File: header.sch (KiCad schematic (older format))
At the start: 43 parts, among them J1 Conn_01x10, J2 Conn_01x08, J3 Conn_01x06, J4 Conn_01x08, Q2 Q_NMOS_GSD, Q3 Q_NMOS_GSD, Q4 Q_NMOS_GSD, SW6 SW_Push, U1 ICE40HX4K-TQ144, U20 MAX11614, U22 MAX40200AUK, U8 TXS0108EPW, U9 TXS0108EPW, Y2 ECS-3225S33-500-FN-TR

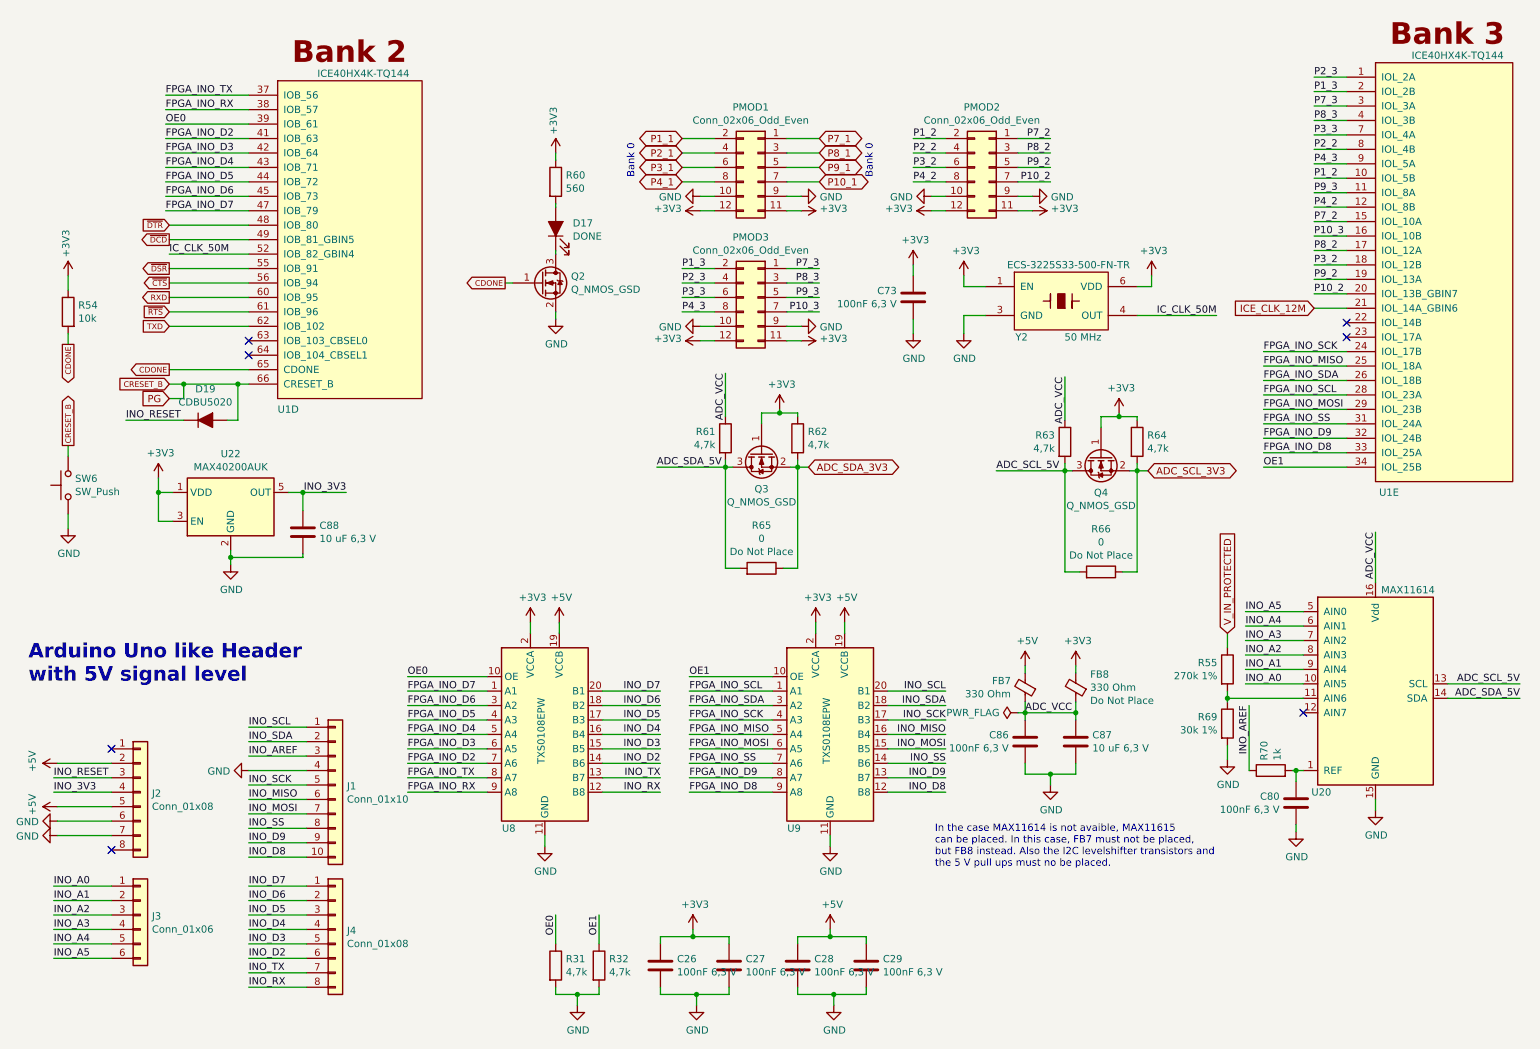
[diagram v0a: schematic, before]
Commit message: Finished Silkscreen and added layer markings as specified by manufacturer
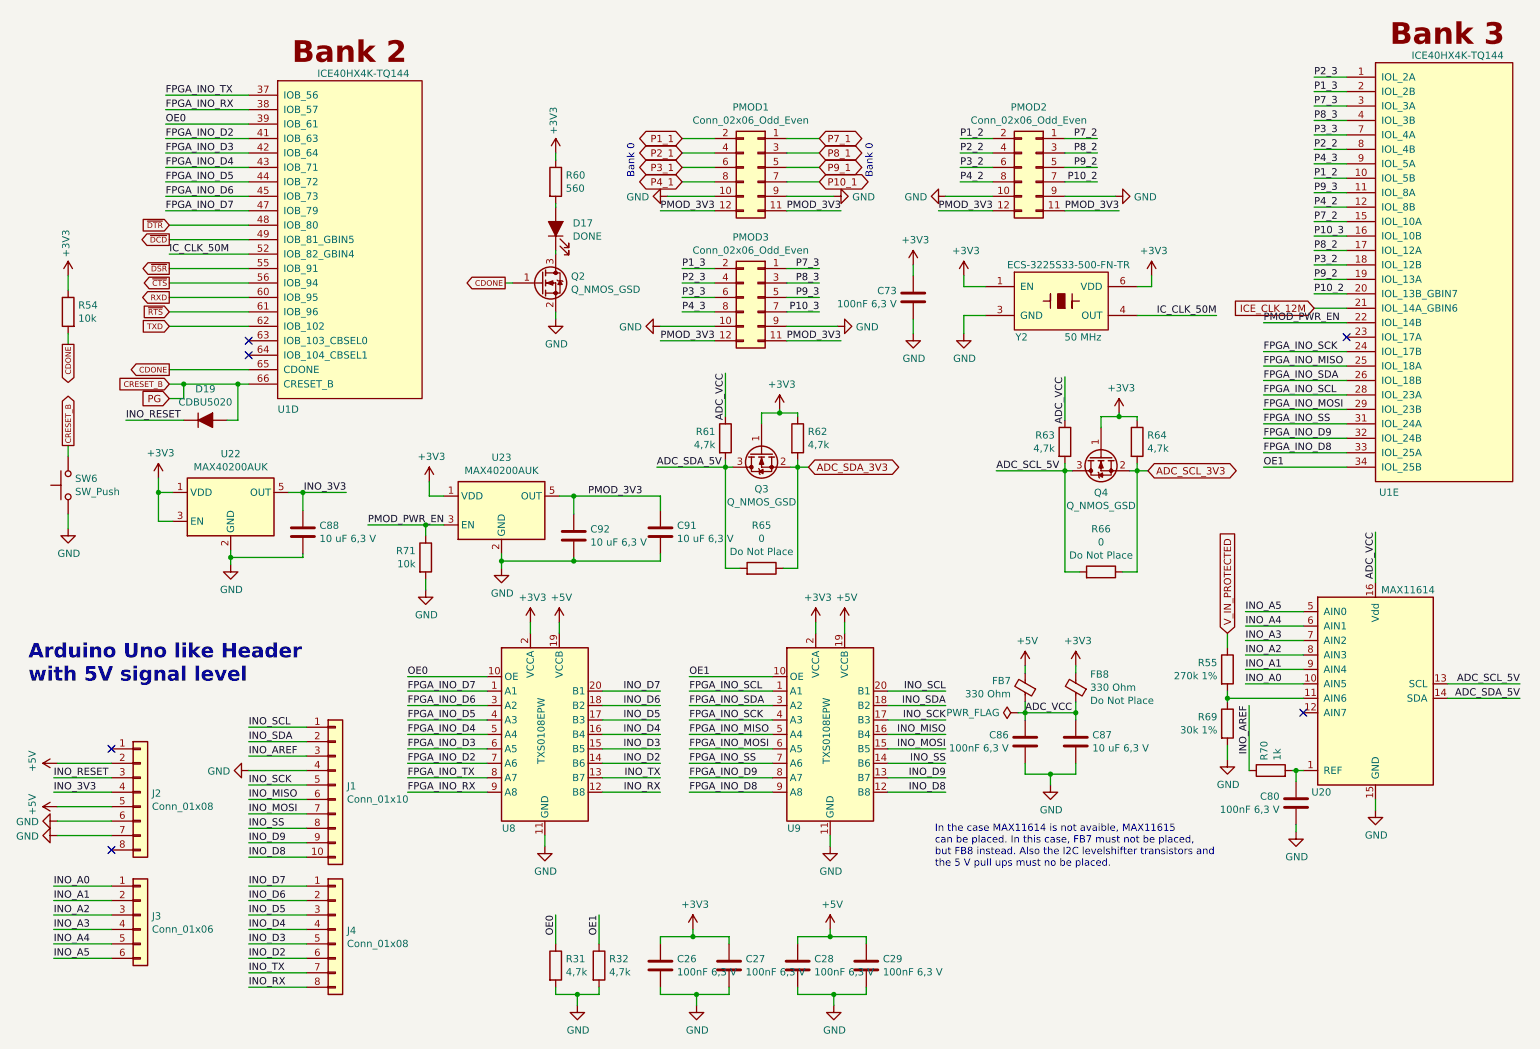
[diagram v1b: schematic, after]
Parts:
- added C91, C92: 10 uF 6,3 V, Capacitor_SMD:C_0603_1608Metric, symbol Device:C
- added R71: 10k, Resistor_SMD:R_0603_1608Metric, symbol Device:R
- added U23: MAX40200AUK, Package_TO_SOT_SMD:SOT-23-5, symbol Analog_Switch:MAX40200AUK
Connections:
- net +3V3: now also U23.1 (VDD); no longer PMOD1.11 (Pin_11), PMOD1.12 (Pin_12), PMOD2.11 (Pin_11), PMOD2.12 (Pin_12), PMOD3.11 (Pin_11), PMOD3.12 (Pin_12)
- net GND: now also C91.2, C92.2, R71.2, U23.2 (GND)
- net PMOD_PWR_EN: now reaches U1.22 (IOL_14B)
- net PMOD_PWR_EN: now also R71.1, U23.3 (EN)
- new net PMOD_3V3: C91.1, C92.1, PMOD1.11 (Pin_11), PMOD1.12 (Pin_12), PMOD2.11 (Pin_11), PMOD2.12 (Pin_12), PMOD3.11 (Pin_11), PMOD3.12 (Pin_12), U23.5 (OUT)
- no-connect marks 7 -> 6
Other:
- moved on the sheet: PMOD2

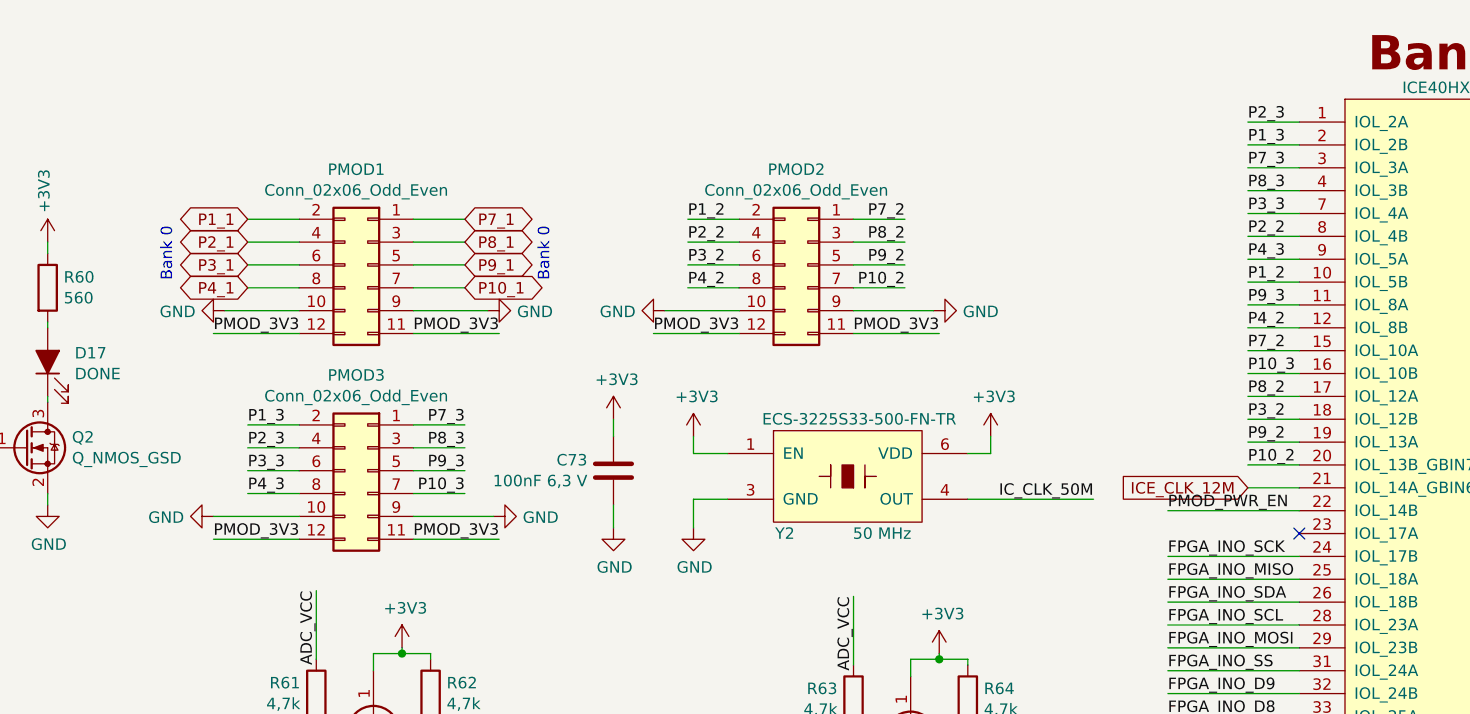
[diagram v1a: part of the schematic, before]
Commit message: Fixed rotated PMODs
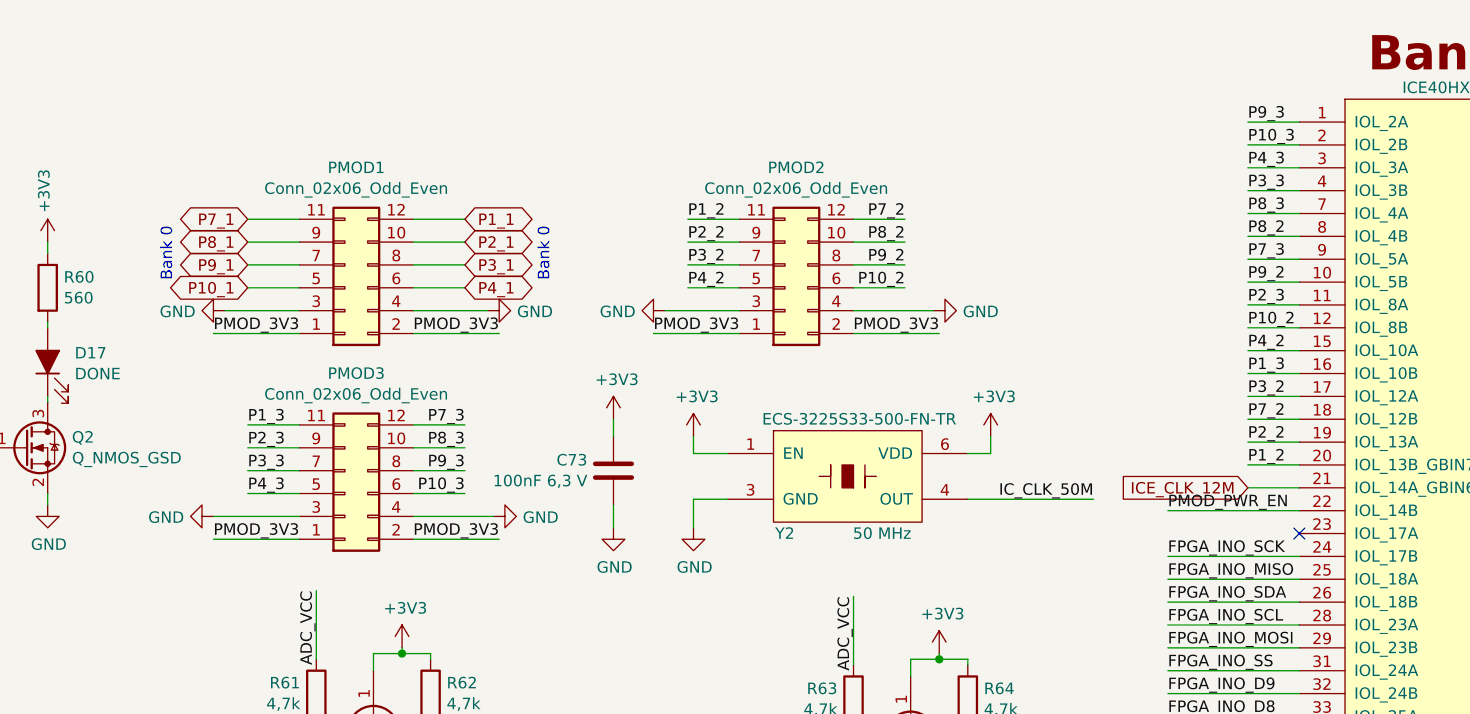
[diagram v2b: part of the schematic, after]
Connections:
- net GND: now also PMOD1.3 (Pin_3), PMOD1.4 (Pin_4), PMOD2.3 (Pin_3), PMOD2.4 (Pin_4), PMOD3.3 (Pin_3), PMOD3.4 (Pin_4); no longer PMOD1.10 (Pin_10), PMOD1.9 (Pin_9), PMOD2.10 (Pin_10), PMOD2.9 (Pin_9), PMOD3.10 (Pin_10), PMOD3.9 (Pin_9)
- net P10_1: now also PMOD1.5 (Pin_5); no longer PMOD1.7 (Pin_7)
- net P10_2: now also PMOD2.6 (Pin_6), U1.12 (IOL_8B); no longer PMOD2.7 (Pin_7), U1.20 (IOL_13B_GBIN7)
- net P10_3: now also PMOD3.6 (Pin_6), U1.2 (IOL_2B); no longer PMOD3.7 (Pin_7), U1.16 (IOL_10B)
- net P1_1: now also PMOD1.12 (Pin_12); no longer PMOD1.2 (Pin_2)
- net P1_2: now also PMOD2.11 (Pin_11), U1.20 (IOL_13B_GBIN7); no longer PMOD2.2 (Pin_2), U1.10 (IOL_5B)
- net P1_3: now also PMOD3.11 (Pin_11), U1.16 (IOL_10B); no longer PMOD3.2 (Pin_2), U1.2 (IOL_2B)
- net P2_1: now also PMOD1.10 (Pin_10); no longer PMOD1.4 (Pin_4)
- net P2_2: now also PMOD2.9 (Pin_9), U1.19 (IOL_13A); no longer PMOD2.4 (Pin_4), U1.8 (IOL_4B)
- net P2_3: now also PMOD3.9 (Pin_9), U1.11 (IOL_8A); no longer PMOD3.4 (Pin_4), U1.1 (IOL_2A)
- net P3_1: now also PMOD1.8 (Pin_8); no longer PMOD1.6 (Pin_6)
- net P3_2: now also PMOD2.7 (Pin_7), U1.17 (IOL_12A); no longer PMOD2.6 (Pin_6), U1.18 (IOL_12B)
- net P3_3: now also PMOD3.7 (Pin_7), U1.4 (IOL_3B); no longer PMOD3.6 (Pin_6), U1.7 (IOL_4A)
- net P4_1: now also PMOD1.6 (Pin_6); no longer PMOD1.8 (Pin_8)
- net P4_2: now also PMOD2.5 (Pin_5), U1.15 (IOL_10A); no longer PMOD2.8 (Pin_8), U1.12 (IOL_8B)
- net P4_3: now also PMOD3.5 (Pin_5), U1.3 (IOL_3A); no longer PMOD3.8 (Pin_8), U1.9 (IOL_5A)
- net P7_1: now also PMOD1.11 (Pin_11); no longer PMOD1.1 (Pin_1)
- net P7_2: now also PMOD2.12 (Pin_12), U1.18 (IOL_12B); no longer PMOD2.1 (Pin_1), U1.15 (IOL_10A)
- net P7_3: now also PMOD3.12 (Pin_12), U1.9 (IOL_5A); no longer PMOD3.1 (Pin_1), U1.3 (IOL_3A)
- net P8_1: now also PMOD1.9 (Pin_9); no longer PMOD1.3 (Pin_3)
- net P8_2: now also PMOD2.10 (Pin_10), U1.8 (IOL_4B); no longer PMOD2.3 (Pin_3), U1.17 (IOL_12A)
- net P8_3: now also PMOD3.10 (Pin_10), U1.7 (IOL_4A); no longer PMOD3.3 (Pin_3), U1.4 (IOL_3B)
- net P9_1: now also PMOD1.7 (Pin_7); no longer PMOD1.5 (Pin_5)
- net P9_2: now also PMOD2.8 (Pin_8), U1.10 (IOL_5B); no longer PMOD2.5 (Pin_5), U1.19 (IOL_13A)
- net P9_3: now also PMOD3.8 (Pin_8), U1.1 (IOL_2A); no longer PMOD3.5 (Pin_5), U1.11 (IOL_8A)
- net PMOD_3V3: now also PMOD1.1 (Pin_1), PMOD1.2 (Pin_2), PMOD2.1 (Pin_1), PMOD2.2 (Pin_2), PMOD3.1 (Pin_1), PMOD3.2 (Pin_2); no longer PMOD1.11 (Pin_11), PMOD1.12 (Pin_12), PMOD2.11 (Pin_11), PMOD2.12 (Pin_12), PMOD3.11 (Pin_11), PMOD3.12 (Pin_12)
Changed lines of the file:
@@
 	0    -1   1    0
 $EndComp
-Wire Wire Line
-	6375 1800 6050 1800
 $Comp
 L power:GND #PWR053
@@
 	5225 1800 5550 1800
 $Comp
-L Connector_Generic:Conn_02x06_Odd_Even PMOD1
-U 1 1 5CD7A9BF
-P 5850 1600
-F 0 "PMOD1" H 5900 2017 50  0000 C CNN
-F 1 "Conn_02x06_Odd_Even" H 5900 1926 50  0000 C CNN
-F 2 "Connector_PinSocket_2.54mm:PinSocket_2x06_P2.54mm_Horizontal" H 5850 1600 50  0001 C CNN
-F 3 "~" H 5850 1600 50  0001 C CNN
-	1    5850 1600
-	-1   0    0    -1
-$EndComp
-Wire Wire Line
-	5325 1400 5550 1400
-Wire Wire Line
-	5325 1500 5550 1500
-Wire Wire Line
-	5325 1600 5550 1600
-Wire Wire Line
-	5325 1700 5550 1700
-Wire Wire Line
-	6275 1400 6050 1400
-Wire Wire Line
-	6275 1500 6050 1500
-Wire Wire Line
-	6275 1600 6050 1600
-Wire Wire Line
-	6275 1700 6050 1700
-$Comp
 L power:GND #PWR056
 U 1 1 5CDD8FE0
@@
 L Connector_Generic:Conn_02x06_Odd_Even PMOD2
 U 1 1 5CDD9002
-P 7775 1600
-F 0 "PMOD2" H 7825 2017 50  0000 C CNN
-F 1 "Conn_02x06_Odd_Even" H 7825 1926 50  0000 C CNN
-F 2 "Connector_PinSocket_2.54mm:PinSocket_2x06_P2.54mm_Horizontal" H 7775 1600 50  0001 C CNN
-F 3 "~" H 7775 1600 50  0001 C CNN
-	1    7775 1600
-	-1   0    0    -1
+P 7675 1700
+F 0 "PMOD2" H 7725 1175 50  0000 C CNN
+F 1 "Conn_02x06_Odd_Even" H 7725 1266 50  0000 C CNN
+F 2 "Connector_PinSocket_2.54mm:PinSocket_2x06_P2.54mm_Horizontal" H 7675 1700 50  0001 C CNN
+F 3 "~" H 7675 1700 50  0001 C CNN
+	1    7675 1700
+	1    0    0    1
 $EndComp
 Wire Wire Line
@@
 L Connector_Generic:Conn_02x06_Odd_Even PMOD3
 U 1 1 5CDF4279
-P 5850 2500
-F 0 "PMOD3" H 5900 2917 50  0000 C CNN
-F 1 "Conn_02x06_Odd_Even" H 5900 2826 50  0000 C CNN
-F 2 "Connector_PinSocket_2.54mm:PinSocket_2x06_P2.54mm_Horizontal" H 5850 2500 50  0001 C CNN
-F 3 "~" H 5850 2500 50  0001 C CNN
-	1    5850 2500
-	-1   0    0    -1
+P 5750 2600
+F 0 "PMOD3" H 5800 2075 50  0000 C CNN
+F 1 "Conn_02x06_Odd_Even" H 5800 2166 50  0000 C CNN
+F 2 "Connector_PinSocket_2.54mm:PinSocket_2x06_P2.54mm_Horizontal" H 5750 2600 50  0001 C CNN
+F 3 "~" H 5750 2600 50  0001 C CNN
+	1    5750 2600
+	1    0    0    1
 $EndComp
 Text Label 5325 2300 0    50   ~ 0
@@
 Wire Wire Line
 	6275 2600 6050 2600
+Text Label 9700 2375 0    50   ~ 0
+P2_2
+Wire Wire Line
+	9700 2375 9925 2375
+Text Label 9700 2175 0    50   ~ 0
+P3_2
+Wire Wire Line
+	9700 2175 9925 2175
+Text Label 9700 1975 0    50   ~ 0
+P4_2
+Wire Wire Line
+	9700 1975 9925 1975
+Text Label 9700 2275 0    50   ~ 0
+P7_2
+Wire Wire Line
+	9700 2275 9925 2275
+Text Label 9700 1475 0    50   ~ 0
+P8_2
+Wire Wire Line
+	9700 1475 9925 1475
 Text Label 9700 1675 0    50   ~ 0
-P1_2
+P9_2
 Wire Wire Line
 	9700 1675 9925 1675
-Text Label 9700 1475 0    50   ~ 0
-P2_2
-Wire Wire Line
-	9700 1475 9925 1475
-Text Label 9700 2275 0    50   ~ 0
-P3_2
-Wire Wire Line
-	9700 2275 9925 2275
-Text Label 9700 1875 0    50   ~ 0
-P4_2
-Wire Wire Line
-	9700 1875 9925 1875
-Text Label 9700 1975 0    50   ~ 0
-P7_2
-Wire Wire Line
-	9700 1975 9925 1975
-Text Label 9700 2175 0    50   ~ 0
-P8_2
-Wire Wire Line
-	9700 2175 9925 2175
-Text Label 9700 2375 0    50   ~ 0
-P9_2
-Wire Wire Line
-	9700 2375 9925 2375
+Text Label 9700 2075 0    50   ~ 0
+P1_3
+Wire Wire Line
+	9700 2075 9925 2075
+Text Label 9700 1775 0    50   ~ 0
+P2_3
+Wire Wire Line
+	9700 1775 9925 1775
+Text Label 9700 1275 0    50   ~ 0
+P3_3
+Wire Wire Line
+	9700 1275 9925 1275
+Text Label 9700 1175 0    50   ~ 0
+P4_3
+Wire Wire Line
+	9700 1175 9925 1175
+Text Label 9700 1575 0    50   ~ 0
+P7_3
+Wire Wire Line
+	9700 1575 9925 1575
+Text Label 9700 1375 0    50   ~ 0
+P8_3
+Wire Wire Line
+	9700 1375 9925 1375
+Text Label 9700 975  0    50   ~ 0
+P9_3
+Wire Wire Line
+	9700 975  9925 975
 Text Label 9700 1075 0    50   ~ 0
-P1_3
+P10_3
 Wire Wire Line
 	9700 1075 9925 1075
-Text Label 9700 975  0    50   ~ 0
-P2_3
-Wire Wire Line
-	9700 975  9925 975
-Text Label 9700 1375 0    50   ~ 0
-P3_3
-Wire Wire Line
-	9700 1375 9925 1375
-Text Label 9700 1575 0    50   ~ 0
-P4_3
-Wire Wire Line
-	9700 1575 9925 1575
-Text Label 9700 1175 0    50   ~ 0
-P7_3
-Wire Wire Line
-	9700 1175 9925 1175
-Text Label 9700 1275 0    50   ~ 0
-P8_3
-Wire Wire Line
-	9700 1275 9925 1275
-Text Label 9700 1775 0    50   ~ 0
-P9_3
-Wire Wire Line
-	9700 1775 9925 1775
-Text Label 9700 2075 0    50   ~ 0
-P10_3
-Wire Wire Line
-	9700 2075 9925 2075
 Text GLabel 1775 2500 0    39   Output ~ 0
 RXD
@@
 Text Label 7250 1400 0    50   ~ 0
 P1_2
-Text GLabel 5325 1400 0    50   BiDi ~ 0
+Text GLabel 6275 1400 2    50   BiDi ~ 0
 P1_1
-Text GLabel 5325 1500 0    50   BiDi ~ 0
+Text GLabel 6275 1500 2    50   BiDi ~ 0
 P2_1
-Text GLabel 5325 1600 0    50   BiDi ~ 0
+Text GLabel 6275 1600 2    50   BiDi ~ 0
 P3_1
-Text GLabel 5325 1700 0    50   BiDi ~ 0
+Text GLabel 6275 1700 2    50   BiDi ~ 0
 P4_1
-Text GLabel 6275 1400 2    50   BiDi ~ 0
-P7_1
-Text GLabel 6275 1500 2    50   BiDi ~ 0
-P8_1
-Text GLabel 6275 1600 2    50   BiDi ~ 0
-P9_1
-Text GLabel 6275 1700 2    50   BiDi ~ 0
-P10_1
 Wire Wire Line
 	2325 2100 1775 2100
@@
 FPGA_INO_D2
 Wire Wire Line
-	9700 2475 9925 2475
-Text Label 9700 2475 0    50   ~ 0
+	9700 1875 9925 1875
+Text Label 9700 1875 0    50   ~ 0
 P10_2
 Text Label 5625 3025 3    50   ~ 0
@@
 Text Label 6425 1900 2    50   ~ 0
 PMOD_3V3
-Wire Wire Line
-	6050 1900 6425 1900
 Text Label 5175 1900 0    50   ~ 0
 PMOD_3V3
@@
 Wire Wire Line
 	3550 4525 3550 4450
+Text GLabel 5325 1700 0    50   BiDi ~ 0
+P10_1
+Text GLabel 5325 1600 0    50   BiDi ~ 0
+P9_1
+Text GLabel 5325 1500 0    50   BiDi ~ 0
+P8_1
+Text GLabel 5325 1400 0    50   BiDi ~ 0
+P7_1
+Wire Wire Line
+	5325 1700 5550 1700
+Wire Wire Line
+	5325 1600 5550 1600
+Wire Wire Line
+	5325 1500 5550 1500
+Wire Wire Line
+	5325 1400 5550 1400
+Wire Wire Line
+	9700 2475 9925 2475
+Text Label 9700 2475 0    50   ~ 0
+P1_2
+Wire Wire Line
+	6275 1600 6050 1600
+Wire Wire Line
+	6275 1700 6050 1700
+Wire Wire Line
+	6375 1800 6050 1800
+Wire Wire Line
+	6050 1900 6425 1900
+Wire Wire Line
+	6275 1400 6050 1400
+Wire Wire Line
+	6275 1500 6050 1500
+$Comp
+L Connector_Generic:Conn_02x06_Odd_Even PMOD1
+U 1 1 5CD7A9BF
+P 5750 1700
+F 0 "PMOD1" H 5800 1175 50  0000 C CNN
+F 1 "Conn_02x06_Odd_Even" H 5800 1266 50  0000 C CNN
+F 2 "Connector_PinSocket_2.54mm:PinSocket_2x06_P2.54mm_Horizontal" H 5750 1700 50  0001 C CNN
+F 3 "~" H 5750 1700 50  0001 C CNN
+	1    5750 1700
+	1    0    0    1
+$EndComp
 $EndSCHEMATC
